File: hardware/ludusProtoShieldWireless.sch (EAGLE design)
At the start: 72 parts, among them Q1 MOSFET-NCHANNELBSS138, Q2 MOSFET-NCHANNELBSS138, U1 XBEE-1XBEE-1_LOCK, U2 ARDUINO, U3 TB6612FNG

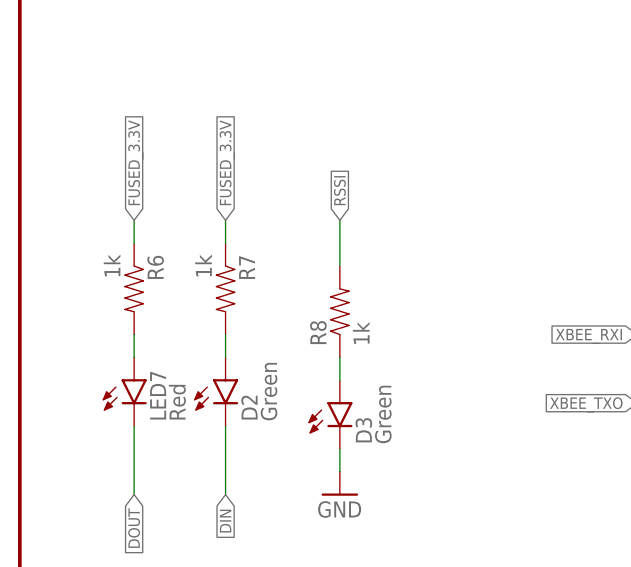
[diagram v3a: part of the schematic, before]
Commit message: Minor Silk changes
Changed the silk on the I2C port so that a rt angle connector does not
block the pin descriptors.

Also changed the DIN / DOUT text on the XBee to RX / TX respectively
from the radio's point of view.
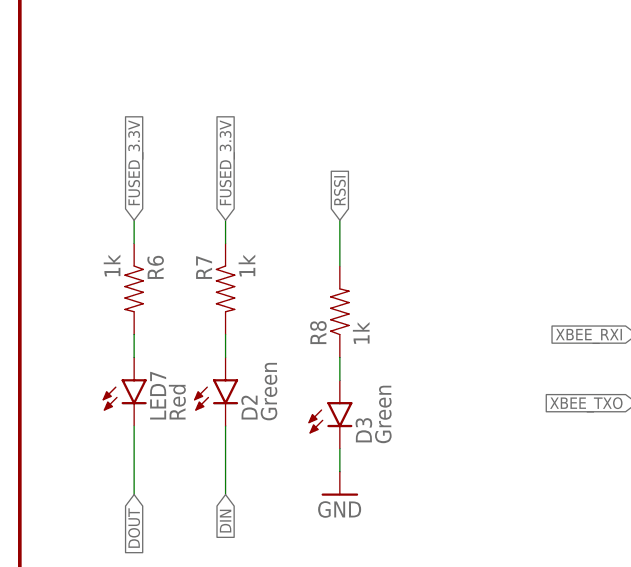
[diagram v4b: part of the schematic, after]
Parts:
- LOGO3: value SFE_LOGO_FLAME.2COP -> SFE_LOGO_FLAME.2EXP; device SparkFun-Aesthetics:SFE_LOGO_FLAME.2COP -> SparkFun-Aesthetics:SFE_LOGO_FLAME.2EXP
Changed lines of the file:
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@@
 <?xml version="1.0" encoding="utf-8"?>
 <!DOCTYPE eagle SYSTEM "eagle.dtd">
-<eagle version="6.5.0">
+<eagle version="7.2.0">
 <drawing>
 <settings>
@@
 <grid distance="0.1" unitdist="inch" unit="inch" style="lines" multiple="1" display="no" altdistance="0.01" altunitdist="inch" altunit="inch"/>
 <layers>
-<layer number="1" name="Top" color="4" fill="1" visible="no" active="no"/>
-<layer number="2" name="Route2" color="1" fill="3" visible="no" active="no"/>
-<layer number="3" name="Route3" color="4" fill="3" visible="no" active="no"/>
-<layer number="4" name="Route4" color="1" fill="4" visible="no" active="no"/>
-<layer number="5" name="Route5" color="4" fill="4" visible="no" active="no"/>
-<layer number="6" name="Route6" color="1" fill="8" visible="no" active="no"/>
-<layer number="7" name="Route7" color="4" fill="8" visible="no" active="no"/>
-<layer number="8" name="Route8" color="1" fill="2" visible="no" active="no"/>
-<layer number="9" name="Route9" color="4" fill="2" visible="no" active="no"/>
-<layer number="10" name="Route10" color="1" fill="7" visible="no" active="no"/>
-<layer number="11" name="Route11" color="4" fill="7" visible="no" active="no"/>
-<layer number="12" name="Route12" color="1" fill="5" visible="no" active="no"/>
-<layer number="13" name="Route13" color="4" fill="5" visible="no" active="no"/>
-<layer number="14" name="Route14" color="1" fill="6" visible="no" active="no"/>
-<layer number="15" name="Route15" color="4" fill="6" visible="no" active="no"/>
-<layer number="16" name="Bottom" color="1" fill="1" visible="no" active="no"/>
-<layer number="17" name="Pads" color="2" fill="1" visible="no" active="no"/>
-<layer number="18" name="Vias" color="2" fill="1" visible="no" active="no"/>
-<layer number="19" name="Unrouted" color="6" fill="1" visible="no" active="no"/>
-<layer number="20" name="Dimension" color="15" fill="1" visible="no" active="no"/>
-<layer number="21" name="tPlace" color="16" fill="1" visible="no" active="no"/>
-<layer number="22" name="bPlace" color="14" fill="1" visible="no" active="no"/>
-<layer number="23" name="tOrigins" color="15" fill="1" visible="no" active="no"/>
-<layer number="24" name="bOrigins" color="15" fill="1" visible="no" active="no"/>
-<layer number="25" name="tNames" color="7" fill="1" visible="no" active="no"/>
-<layer number="26" name="bNames" color="7" fill="1" visible="no" active="no"/>
-<layer number="27" name="tValues" color="7" fill="1" visible="no" active="no"/>
-<layer number="28" name="bValues" color="7" fill="1" visible="no" active="no"/>
+<layer number="1" name="Top" color="4" fill="1" visible="yes" active="no"/>
+<layer number="2" name="Route2" color="1" fill="3" visible="yes" active="no"/>
+<layer number="3" name="Route3" color="4" fill="3" visible="yes" active="no"/>
+<layer number="4" name="Route4" color="1" fill="4" visible="yes" active="no"/>
+<layer number="5" name="Route5" color="4" fill="4" visible="yes" active="no"/>
+<layer number="6" name="Route6" color="1" fill="8" visible="yes" active="no"/>
+<layer number="7" name="Route7" color="4" fill="8" visible="yes" active="no"/>
+<layer number="8" name="Route8" color="1" fill="2" visible="yes" active="no"/>
+<layer number="9" name="Route9" color="4" fill="2" visible="yes" active="no"/>
+<layer number="10" name="Route10" color="1" fill="7" visible="yes" active="no"/>
+<layer number="11" name="Route11" color="4" fill="7" visible="yes" active="no"/>
+<layer number="12" name="Route12" color="1" fill="5" visible="yes" active="no"/>
+<layer number="13" name="Route13" color="4" fill="5" visible="yes" active="no"/>
+<layer number="14" name="Route14" color="1" fill="6" visible="yes" active="no"/>
+<layer number="15" name="Route15" color="4" fill="6" visible="yes" active="no"/>
+<layer number="16" name="Bottom" color="1" fill="1" visible="yes" active="no"/>
+<layer number="17" name="Pads" color="2" fill="1" visible="yes" active="no"/>
+<layer number="18" name="Vias" color="2" fill="1" visible="yes" active="no"/>
+<layer number="19" name="Unrouted" color="6" fill="1" visible="yes" active="no"/>
+<layer number="20" name="Dimension" color="15" fill="1" visible="yes" active="no"/>
+<layer number="21" name="tPlace" color="16" fill="1" visible="yes" active="no"/>
+<layer number="22" name="bPlace" color="14" fill="1" visible="yes" active="no"/>
+<layer number="23" name="tOrigins" color="15" fill="1" visible="yes" active="no"/>
+<layer number="24" name="bOrigins" color="15" fill="1" visible="yes" active="no"/>
+<layer number="25" name="tNames" color="7" fill="1" visible="yes" active="no"/>
+<layer number="26" name="bNames" color="7" fill="1" visible="yes" active="no"/>
+<layer number="27" name="tValues" color="7" fill="1" visible="yes" active="no"/>
+<layer number="28" name="bValues" color="7" fill="1" visible="yes" active="no"/>
 <layer number="29" name="tStop" color="7" fill="3" visible="no" active="no"/>
 <layer number="30" name="bStop" color="7" fill="6" visible="no" active="no"/>
@@
 <layer number="35" name="tGlue" color="7" fill="4" visible="no" active="no"/>
 <layer number="36" name="bGlue" color="7" fill="5" visible="no" active="no"/>
-<layer number="37" name="tTest" color="7" fill="1" visible="no" active="no"/>
-<layer number="38" name="bTest" color="7" fill="1" visible="no" active="no"/>
+<layer number="37" name="tTest" color="7" fill="1" visible="yes" active="no"/>
+<layer number="38" name="bTest" color="7" fill="1" visible="yes" active="no"/>
 <layer number="39" name="tKeepout" color="4" fill="11" visible="no" active="no"/>
 <layer number="40" name="bKeepout" color="1" fill="11" visible="no" active="no"/>
@@
 <layer number="44" name="Drills" color="7" fill="1" visible="no" active="no"/>
 <layer number="45" name="Holes" color="7" fill="1" visible="no" active="no"/>
-<layer number="46" name="Milling" color="3" fill="1" visible="no" active="no"/>
-<layer number="47" name="Measures" color="7" fill="1" visible="no" active="no"/>
-<layer number="48" name="Document" color="7" fill="1" visible="no" active="no"/>
-<layer number="49" name="Reference" color="7" fill="1" visible="no" active="no"/>
-<layer number="50" name="dxf" color="7" fill="1" visible="no" active="no"/>
-<layer number="51" name="tDocu" color="6" fill="1" visible="no" active="no"/>
-<layer number="52" name="bDocu" color="7" fill="1" visible="no" active="no"/>
-<layer number="53" name="tGND_GNDA" color="7" fill="9" visible="no" active="no"/>
-<layer number="54" name="bGND_GNDA" color="1" fill="9" visible="no" active="no"/>
-<layer number="56" name="wert" color="7" fill="1" visible="no" active="no"/>
-<layer number="57" name="tCAD" color="7" fill="1" visible="no" active="no"/>
+<layer number="46" name="Milling" color="3" fill="1" visible="yes" active="no"/>
+<layer number="47" name="Measures" color="7" fill="1" visible="yes" active="no"/>
+<layer number="48" name="Document" color="7" fill="1" visible="yes" active="no"/>
+<layer number="49" name="Reference" color="7" fill="1" visible="yes" active="no"/>
+<layer number="50" name="dxf" color="7" fill="1" visible="yes" active="no"/>
+<layer number="51" name="tDocu" color="6" fill="1" visible="yes" active="no"/>
+<layer number="52" name="bDocu" color="7" fill="1" visible="yes" active="no"/>
+<layer number="53" name="tGND_GNDA" color="7" fill="9" visible="yes" active="no"/>
+<layer number="54" name="bGND_GNDA" color="1" fill="9" visible="yes" active="no"/>
+<layer number="56" name="wert" color="7" fill="1" visible="yes" active="no"/>
+<layer number="57" name="tCAD" color="7" fill="1" visible="yes" active="no"/>
 <layer number="90" name="Modules" color="5" fill="1" visible="no" active="yes"/>
 <layer number="91" name="Nets" color="2" fill="1" visible="yes" active="yes"/>
@@
 <part name="LOGO1" library="SparkFun-Aesthetics" deviceset="OSHW-LOGO" device="M"/>
 <part name="LOGO2" library="SparkFun-Aesthetics" deviceset="SFE_LOGO_NAME_FLAME" device=".1_INCH" value="SFE_LOGO_NAME_FLAME.1_INCH"/>
-<part name="LOGO3" library="SparkFun-Aesthetics" deviceset="SFE_LOGO_FLAME" device=".2COP"/>
+<part name="LOGO3" library="SparkFun-Aesthetics" deviceset="SFE_LOGO_FLAME" device=".2EXP" value="SFE_LOGO_FLAME.2EXP"/>
 <part name="LOGO4" library="SparkFun-Aesthetics" deviceset="SFE_LOGO_NAME_FLAME" device=".1_INCH" value="SFE_LOGO_NAME_FLAME.1_INCH"/>
 <part name="JP22" library="SparkFun-Connectors" deviceset="M04" device="LOCK"/>
@@
 <instance part="D2" gate="G$1" x="22.86" y="43.18"/>
 <instance part="R6" gate="G$1" x="12.7" y="53.34" rot="R270"/>
-<instance part="R7" gate="G$1" x="22.86" y="53.34" rot="R270"/>
+<instance part="R7" gate="G$1" x="22.86" y="53.34" rot="MR270"/>
 <instance part="D3" gate="G$1" x="35.56" y="40.64"/>
 <instance part="R8" gate="G$1" x="35.56" y="50.8" rot="R90"/>
